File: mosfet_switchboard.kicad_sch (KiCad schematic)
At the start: 6 parts, among them J1 Power Input, J2 Conn_01x02_Male, J3 Power Output, Q1 DMP3013SFV, U1 ZXGD3006E6

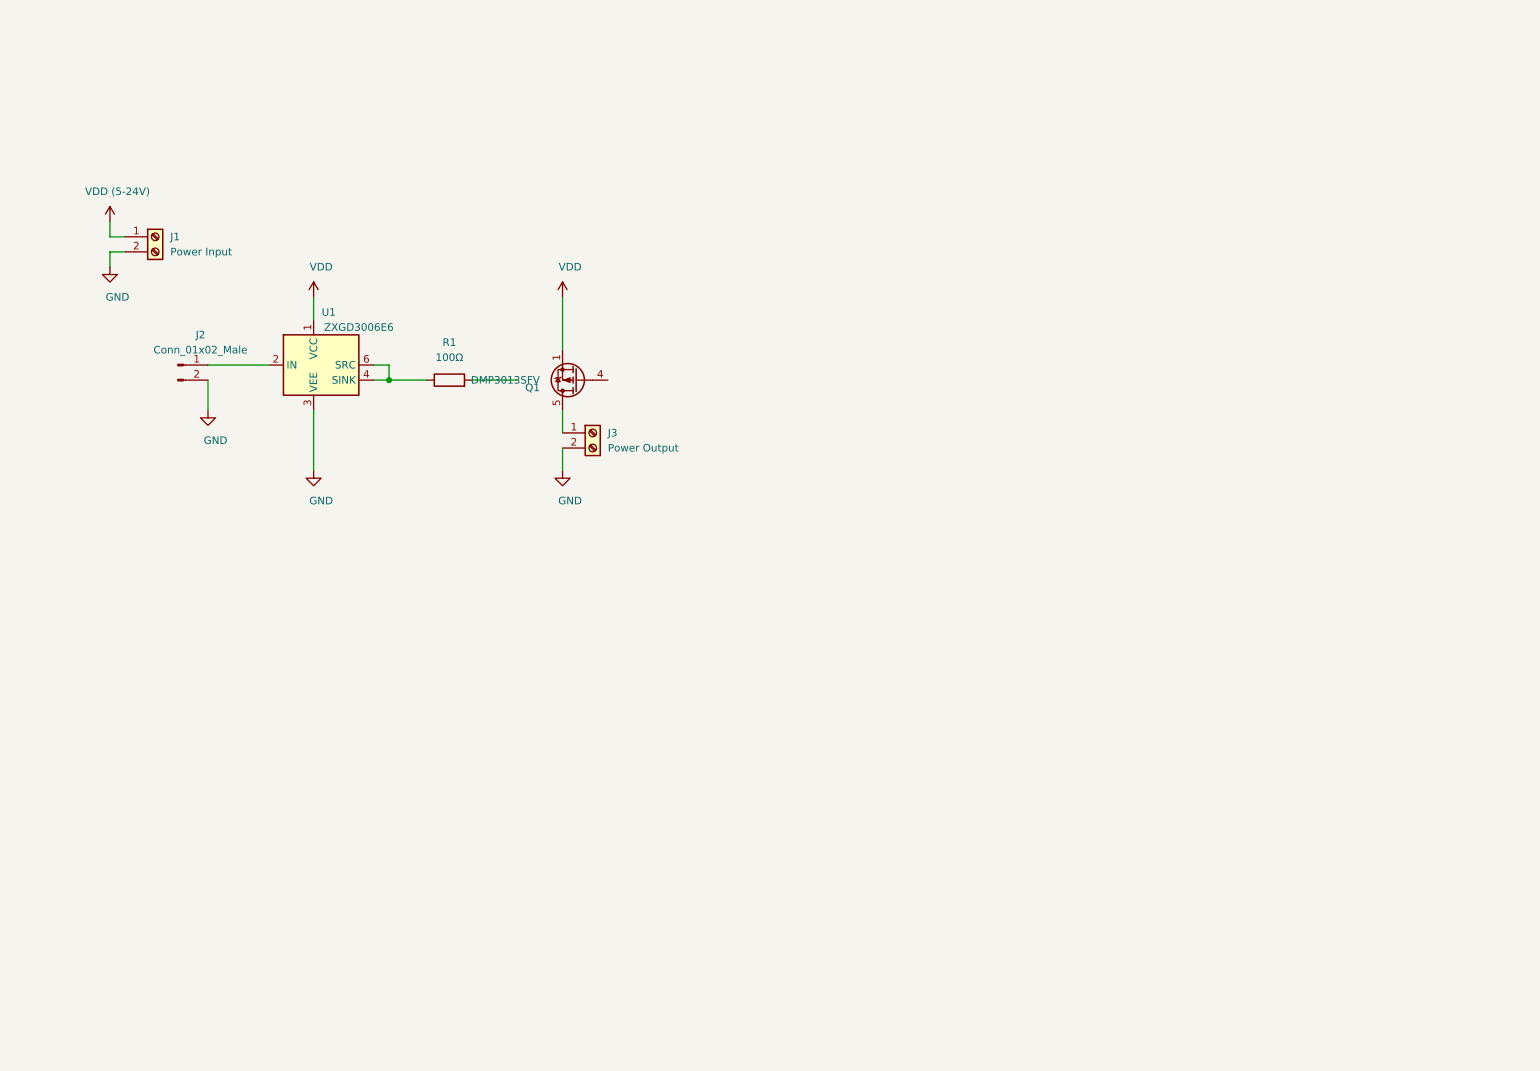
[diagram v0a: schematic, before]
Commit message: initial version with STM32, before splitup
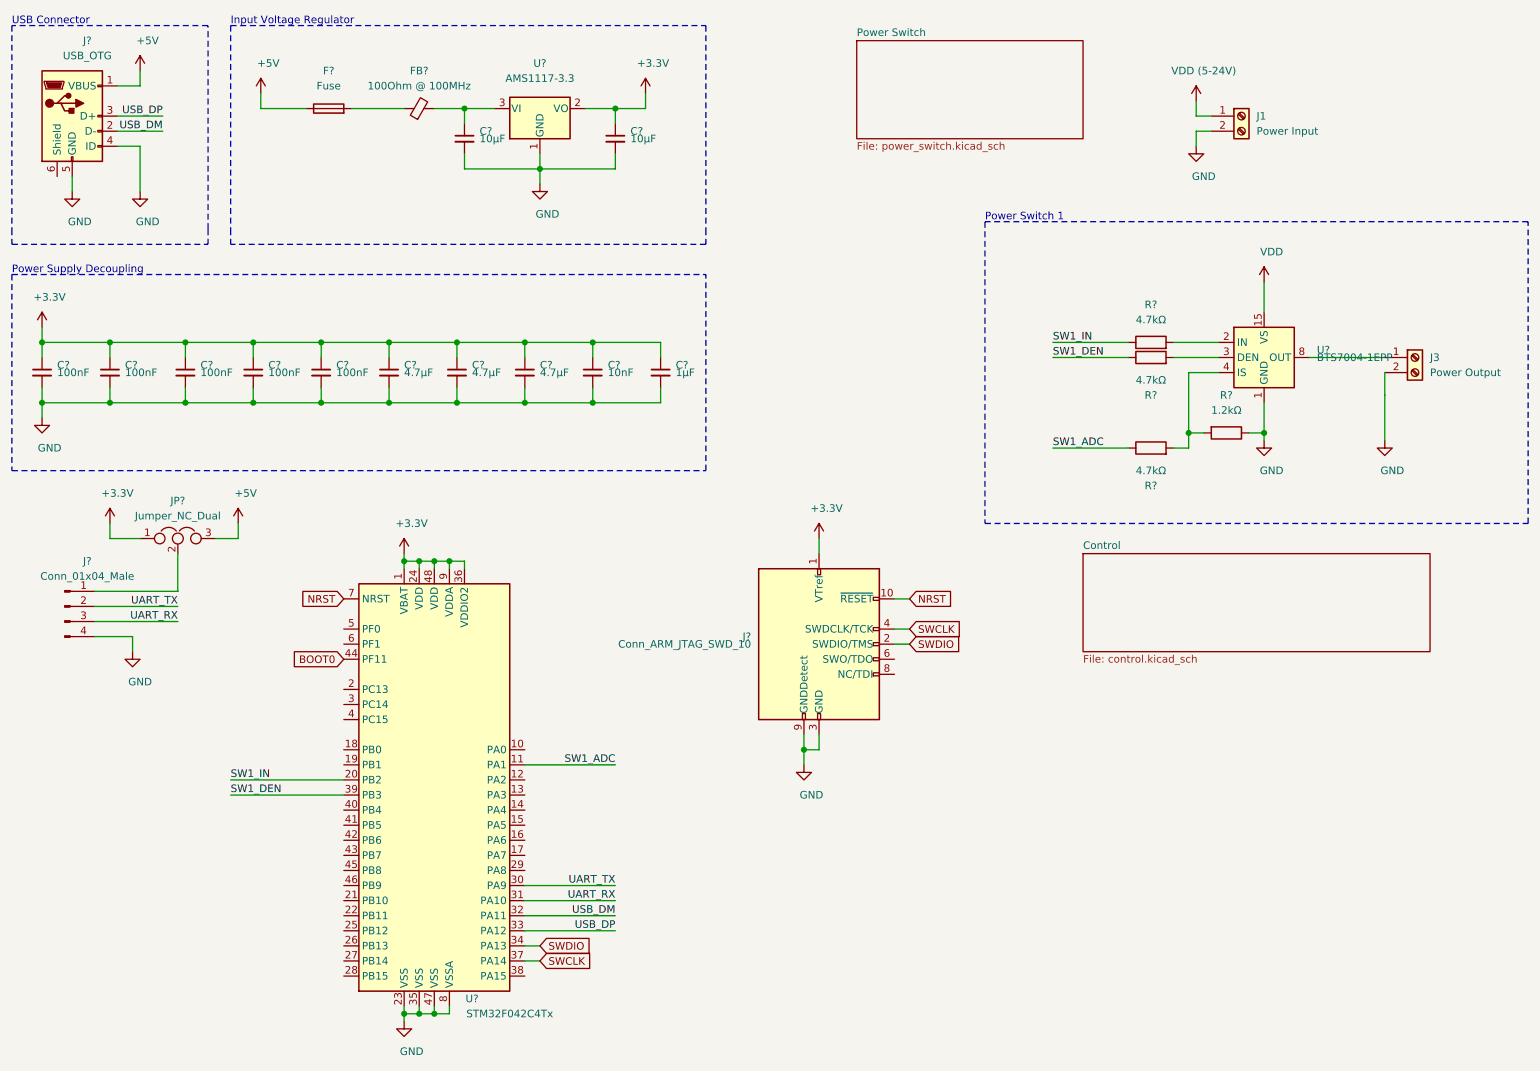
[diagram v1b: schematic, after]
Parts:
- removed J2: Conn_01x02_Male, Connector_PinSocket_2.54mm:PinSocket_1x02_P2.54mm_Vertical, symbol Connector:Conn_01x02_Male
- removed Q1: DMP3013SFV, Package_SON:Diodes_PowerDI3333-8, symbol Transistor_FET:DMP3013SFV
- removed R1: 100Ω, Resistor_SMD:R_0402_1005Metric, symbol Device:R
- removed U1: ZXGD3006E6, Package_TO_SOT_SMD:SOT-23-6, symbol Driver_FET:ZXGD3006E6
- added C? (x5): 100nF, symbol Device:C_Small
- added C? (x3): 4.7µF, symbol Device:C_Small
- added C?: 10nF, symbol Device:C_Small
- added C? (x2): 10µF, symbol Device:C_Small
- added C?: 1µF, symbol Device:C_Small
- added F?: Fuse, symbol Device:Fuse
- added FB?: 100Ohm @ 100MHz, symbol Device:Ferrite_Bead_Small
- added J?: Conn_01x04_Male, symbol Connector:Conn_01x04_Male
- added J?: Conn_ARM_JTAG_SWD_10, symbol Connector:Conn_ARM_JTAG_SWD_10
- added J?: USB_OTG, symbol Connector:USB_OTG
- added JP?: Jumper_NC_Dual, symbol Device:Jumper_NC_Dual
- added R? (x3): 4.7kΩ, symbol Device:R
- added R?: 1.2kΩ, symbol Device:R
- added U?: BTS7004-1EPP, Package_SO:Infineon_PG-TSDSO-14-22, symbol Power_Management:BTS7004-1EPP
- added U?: AMS1117-3.3, Package_TO_SOT_SMD:SOT-223-3_TabPin2, symbol Regulator_Linear:AMS1117-3.3
- added U?: STM32F042C4Tx, Package_QFP:LQFP-48_7x7mm_P0.5mm, symbol MCU_ST_STM32F0:STM32F042C4Tx
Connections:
- net GND: now also C?.2, C?.2, C?.2, C?.2, C?.2, C?.2, C?.2, C?.2, C?.2, C?.2, C?.2, C?.2, J?.3 (GND), J?.4 (ID), J?.4 (Pin_4), J?.5 (GND), J?.5 (GND), J?.9 (GNDDetect), R?.1, U?.1 (GND), U?.1 (GND), U?.23 (VSS), U?.35 (VSS), U?.47 (VSS), U?.8 (VSSA)
- net VDD: now also U?.15 (VS)
- net at J3.1 (Pin_1): now also U?.10 (OUT), U?.12 (OUT), U?.13 (OUT), U?.14 (OUT), U?.8 (OUT), U?.9 (OUT)
- new net: R?.2, U?.2 (IN)
- new net: R?.2, U?.3 (DEN)
- new net: R?.2, R?.2, U?.4 (IS)
- new net: J?.1 (Pin_1), JP?.2
- new net: C?.1, FB?.2, U?.3 (VI)
- new net: F?.2, FB?.1
- new net +3V3: C?.1, C?.1, C?.1, C?.1, C?.1, C?.1, C?.1, C?.1, C?.1, C?.1, C?.1, J?.1 (VTref), JP?.1, U?.1 (VBAT), U?.2 (VO), U?.24 (VDD), U?.36 (VDDIO2), U?.48 (VDD), U?.9 (VDDA)
- new net +5V: F?.1, J?.1 (VBUS), JP?.3
- new net BOOT0: U?.44 (PF11)
- new net NRST: J?.10 (~RESET~), U?.7 (NRST)
- new net SW1_ADC: R?.1, U?.11 (PA1)
- new net SW1_DEN: R?.1, U?.39 (PB3)
- new net SW1_IN: R?.1, U?.20 (PB2)
- new net SWCLK: J?.4 (SWDCLK/TCK), U?.37 (PA14)
- new net SWDIO: J?.2 (SWDIO/TMS), U?.34 (PA13)
- new net UART_RX: J?.3 (Pin_3), U?.31 (PA10)
- new net UART_TX: J?.2 (Pin_2), U?.30 (PA9)
- new net USB_DM: J?.2 (D-), U?.32 (PA11)
- new net USB_DP: J?.3 (D+), U?.33 (PA12)
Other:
- added sheet Control (control.kicad_sch)
- added sheet Power Switch (power_switch.kicad_sch)
- note added: "Input Voltage Regulator"
- note added: "Power Supply Decoupling"
- note added: "Power Switch 1"
- note added: "USB Connector"
- moved on the sheet: J1, J3

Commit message: split into multiple sheets
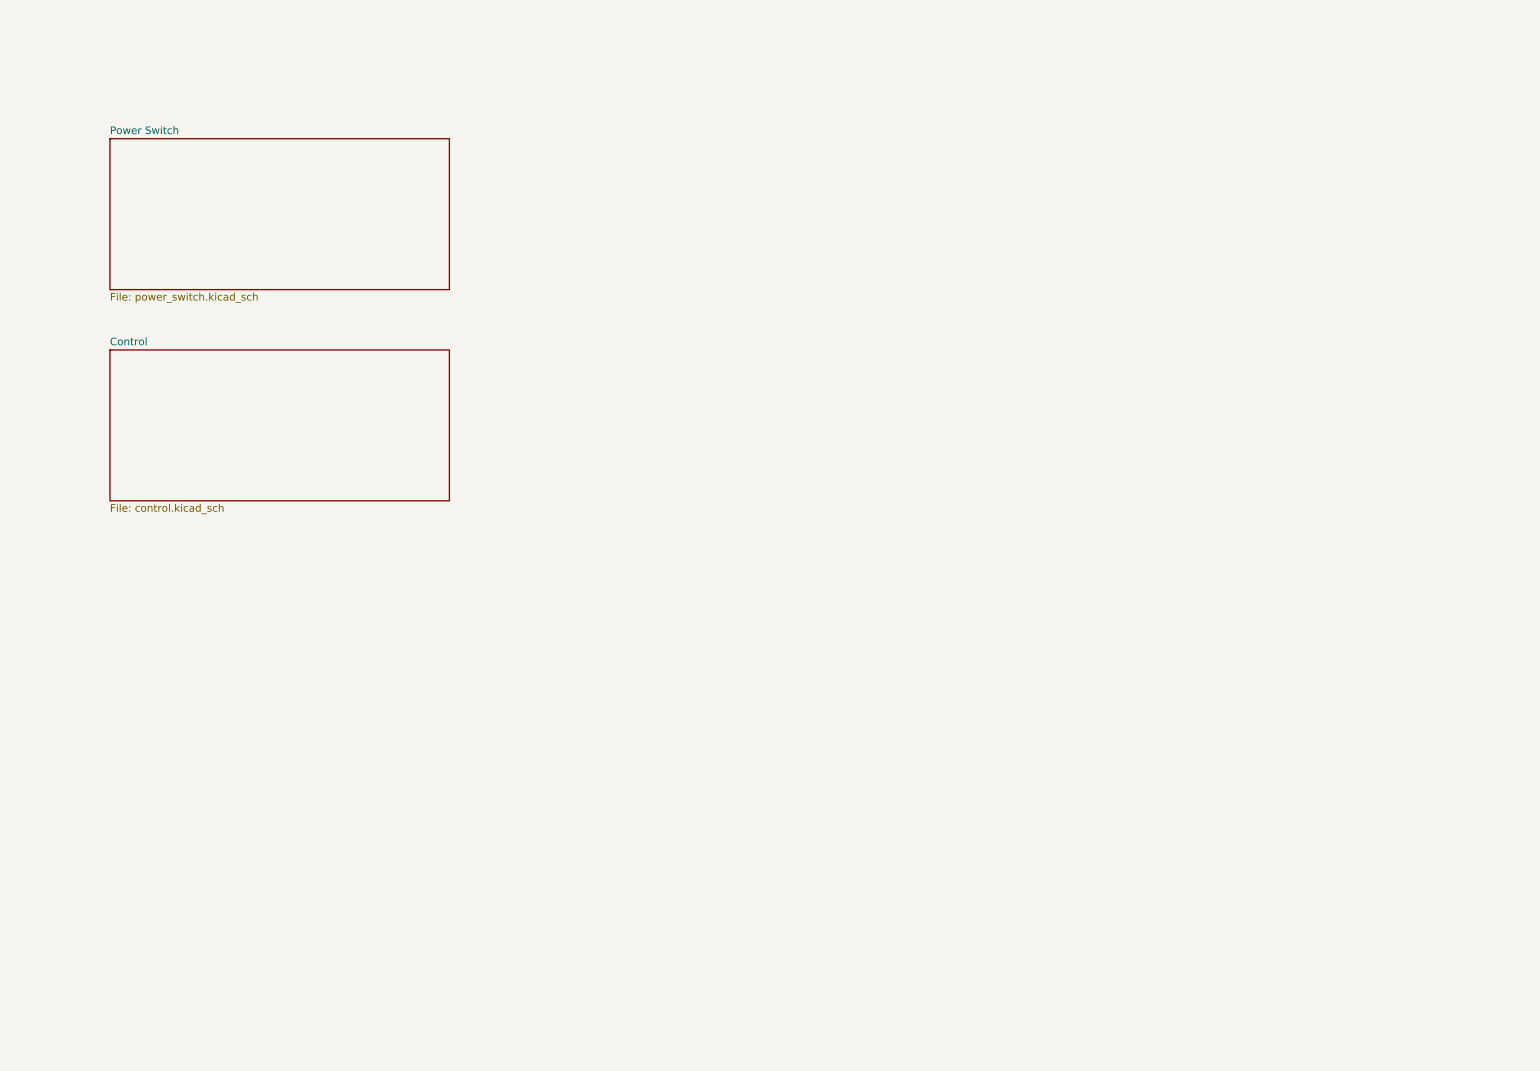
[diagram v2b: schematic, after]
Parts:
- removed C? (x5): 100nF, symbol Device:C_Small
- removed C? (x3): 4.7µF, symbol Device:C_Small
- removed C?: 10nF, symbol Device:C_Small
- removed C? (x2): 10µF, symbol Device:C_Small
- removed C?: 1µF, symbol Device:C_Small
- removed F?: Fuse, symbol Device:Fuse
- removed FB?: 100Ohm @ 100MHz, symbol Device:Ferrite_Bead_Small
- removed J1: Power Input, TerminalBlock_RND:TerminalBlock_RND_205-00287_1x02_P5.08mm_Horizontal, symbol Connector:Screw_Terminal_01x02
- removed J3: Power Output, TerminalBlock_RND:TerminalBlock_RND_205-00287_1x02_P5.08mm_Horizontal, symbol Connector:Screw_Terminal_01x02
- removed J?: Conn_01x04_Male, symbol Connector:Conn_01x04_Male
- removed J?: Conn_ARM_JTAG_SWD_10, symbol Connector:Conn_ARM_JTAG_SWD_10
- removed J?: USB_OTG, symbol Connector:USB_OTG
- removed JP?: Jumper_NC_Dual, symbol Device:Jumper_NC_Dual
- removed R? (x3): 4.7kΩ, symbol Device:R
- removed R?: 1.2kΩ, symbol Device:R
- removed U?: BTS7004-1EPP, Package_SO:Infineon_PG-TSDSO-14-22, symbol Power_Management:BTS7004-1EPP
- removed U?: AMS1117-3.3, Package_TO_SOT_SMD:SOT-223-3_TabPin2, symbol Regulator_Linear:AMS1117-3.3
- removed U?: STM32F042C4Tx, Package_QFP:LQFP-48_7x7mm_P0.5mm, symbol MCU_ST_STM32F0:STM32F042C4Tx
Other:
- note removed: "Input Voltage Regulator"
- note removed: "Power Supply Decoupling"
- note removed: "Power Switch 1"
- note removed: "USB Connector"

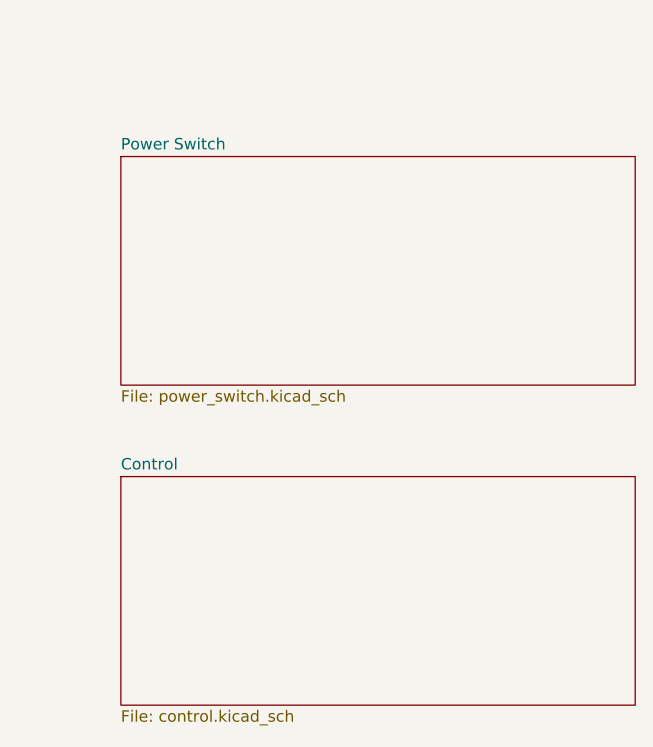
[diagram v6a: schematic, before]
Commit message: introduce hierarchical sheets for power switches
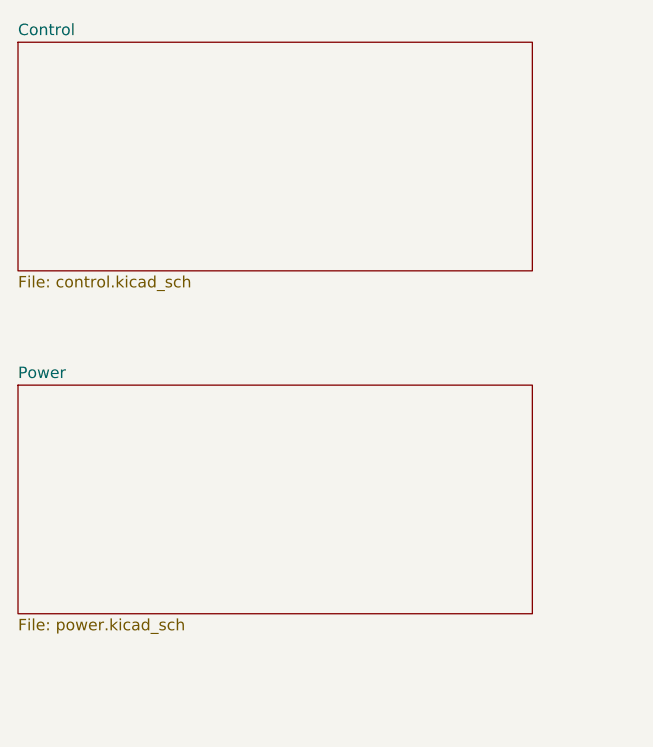
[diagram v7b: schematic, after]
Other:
- removed sheet Power Switch
- added sheet Power (power.kicad_sch)
